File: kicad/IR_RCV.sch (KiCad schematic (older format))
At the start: 9 parts, among them J1 Host, J2 Slave, Q1 MTM231232LBF, Q2 DMN3065LW-7, Q3 SFH3015FA

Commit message: 部品を配置 kicad5
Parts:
- removed J1: Host, mouse:STAND_HOST_05, symbol Conn_01x05_Female
- removed J2: Slave, mouse:STAND_SLAVE_05, symbol Conn_01x05_Male
- added J15: Host, mouse:STAND_HOST_05, symbol Connector:Conn_01x05_Female
- added J16: Slave, mouse:STAND_SLAVE_05, symbol Connector:Conn_01x05_Male
- C6: symbol C -> Device:C
- D3: symbol LED -> Device:LED
- Q1: symbol Q_PMOS_GSD -> Device:Q_PMOS_GSD
- Q2: symbol Q_NMOS_GSD -> Device:Q_NMOS_GSD
- Q3: symbol Q_Photo_NPN -> Device:Q_Photo_NPN
- R6, R7: symbol R -> Device:R
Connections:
- net +3V3: now also J15.1 (Pin_1)
- net GND: now also J15.5 (Pin_5)
- net IR_LED: now also J15.3 (Pin_3)
- net IR_RCV: now also J15.4 (Pin_4)
- net VDDA: now also J15.2 (Pin_2)
- net s_3.3V: now also J16.1 (Pin_1)
- net s_AVDD: now also J16.2 (Pin_2)
- net s_GND: now also J16.5 (Pin_5)
- net s_IR_LED: now also J16.3 (Pin_3)
- net s_IR_RCV: now also J16.4 (Pin_4)
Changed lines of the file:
@@
-EESchema Schematic File Version 2
-LIBS:power
-LIBS:device
-LIBS:transistors
-LIBS:conn
-LIBS:linear
-LIBS:regul
-LIBS:74xx
-LIBS:cmos4000
-LIBS:adc-dac
-LIBS:memory
-LIBS:xilinx
-LIBS:microcontrollers
-LIBS:dsp
-LIBS:microchip
-LIBS:analog_switches
-LIBS:motorola
-LIBS:texas
-LIBS:intel
-LIBS:audio
-LIBS:interface
-LIBS:digital-audio
-LIBS:philips
-LIBS:display
-LIBS:cypress
-LIBS:siliconi
-LIBS:opto
-LIBS:atmel
-LIBS:contrib
-LIBS:valves
-LIBS:KERISE
-LIBS:74xgxx
-LIBS:ac-dc
-LIBS:actel
-LIBS:allegro
-LIBS:Altera
-LIBS:analog_devices
-LIBS:battery_management
-LIBS:bbd
-LIBS:bosch
-LIBS:brooktre
-LIBS:cmos_ieee
-LIBS:dc-dc
-LIBS:diode
-LIBS:elec-unifil
-LIBS:ESD_Protection
-LIBS:ftdi
-LIBS:gennum
-LIBS:hc11
-LIBS:ir
-LIBS:Lattice
-LIBS:leds
-LIBS:maxim
-LIBS:mechanical
-LIBS:microchip_dspic33dsc
-LIBS:microchip_pic10mcu
-LIBS:microchip_pic12mcu
-LIBS:microchip_pic16mcu
-LIBS:microchip_pic18mcu
-LIBS:microchip_pic24mcu
-LIBS:microchip_pic32mcu
-LIBS:modules
-LIBS:motor_drivers
-LIBS:motors
-LIBS:msp430
-LIBS:nordicsemi
-LIBS:nxp
-LIBS:nxp_armmcu
-LIBS:onsemi
-LIBS:Oscillators
-LIBS:Power_Management
-LIBS:powerint
-LIBS:pspice
-LIBS:references
-LIBS:relays
-LIBS:rfcom
-LIBS:sensors
-LIBS:silabs
-LIBS:stm8
-LIBS:stm32
-LIBS:supertex
-LIBS:switches
-LIBS:transf
-LIBS:triac_thyristor
-LIBS:ttl_ieee
-LIBS:video
-LIBS:wiznet
-LIBS:Worldsemi
-LIBS:Xicor
-LIBS:zetex
-LIBS:Zilog
-LIBS:graphic_symbols
-LIBS:infineon
-LIBS:intersil
-LIBS:LEM
-LIBS:logic_programmable
-LIBS:RFSolutions
+EESchema Schematic File Version 4
 LIBS:KERISE-cache
-EELAYER 25 0
+EELAYER 26 0
 EELAYER END
 $Descr A4 11693 8268
 encoding utf-8
-Sheet 13 15
+Sheet 12 14
 Title ""
 Date ""
@@
 Photo Reflector v20180503\nKERI's Lab
 $Comp
-L Q_NMOS_GSD Q2
+L Device:Q_NMOS_GSD Q2
 U 1 1 589BE75A
 P 4300 5500
@@
 AR Path="/597E1B35/589BE75A" Ref="Q9"  Part="1"
 AR Path="/597E1B39/589BE75A" Ref="Q12"  Part="1"
-F 0 "Q5" H 4300 5650 50  0000 R CNN
+F 0 "Q12" H 4300 5650 50  0000 R CNN
 F 1 "DMN3065LW-7" H 4350 5350 50  0000 R CNN
 F 2 "TO_SOT_Packages_SMD:SOT-323_SC-70" H 4500 5600 50  0001 C CNN
@@
 $EndComp
 $Comp
-L R R6
+L Device:R R6
 U 1 1 589BE76D
 P 4400 4450
 AR Path="/57CF0B09/589BE76D" Ref="R6"  Part="1"
 AR Path="/57CF2A30/589BE76D" Ref="R8"  Part="1"
-AR Path="/597E1B35/589BE76D" Ref="R13"  Part="1"
-AR Path="/597E1B39/589BE76D" Ref="R15"  Part="1"
-F 0 "R8" V 4480 4450 50  0000 C CNN
+AR Path="/597E1B35/589BE76D" Ref="R11"  Part="1"
+AR Path="/597E1B39/589BE76D" Ref="R13"  Part="1"
+F 0 "R13" V 4480 4450 50  0000 C CNN
 F 1 "100" V 4400 4450 50  0000 C CNN
 F 2 "Resistors_SMD:R_0603" V 4330 4450 50  0001 C CNN
@@
 IR_LED
 $Comp
-L GND #PWR036
+L power:GND #PWR035
 U 1 1 589BF265
 P 4400 2600
-AR Path="/57CF0B09/589BF265" Ref="#PWR036"  Part="1"
-AR Path="/57CF2A30/589BF265" Ref="#PWR039"  Part="1"
-AR Path="/597E1B35/589BF265" Ref="#PWR063"  Part="1"
-AR Path="/597E1B39/589BF265" Ref="#PWR066"  Part="1"
-F 0 "#PWR066" H 4400 2350 50  0001 C CNN
+AR Path="/57CF0B09/589BF265" Ref="#PWR035"  Part="1"
+AR Path="/57CF2A30/589BF265" Ref="#PWR038"  Part="1"
+AR Path="/597E1B35/589BF265" Ref="#PWR054"  Part="1"
+AR Path="/597E1B39/589BF265" Ref="#PWR057"  Part="1"
+F 0 "#PWR057" H 4400 2350 50  0001 C CNN
 F 1 "GND" H 4400 2450 50  0000 C CNN
 F 2 "" H 4400 2600 50  0000 C CNN
@@
 	4100 2000 4100 2200
 Wire Wire Line
-	4400 4800 4400 4600
+	4400 4800 4400 4700
 Wire Wire Line
 	5600 5700 5600 6000
@@
 s_AVDD
 $Comp
-L LED D3
+L Device:LED D3
 U 1 1 594AC674
 P 4400 4950
@@
 AR Path="/597E1B35/594AC674" Ref="D5"  Part="1"
 AR Path="/597E1B39/594AC674" Ref="D6"  Part="1"
-F 0 "D4" V 4500 4800 50  0000 C CNN
+F 0 "D6" V 4500 4800 50  0000 C CNN
 F 1 "SFH4045N" V 4400 4650 50  0000 C CNN
 F 2 "mouse:SFH4045N" H 4400 4950 50  0001 C CNN
@@
 $EndComp
 $Comp
-L VDDA #PWR037
+L power:VDDA #PWR033
 U 1 1 59C54857
 P 4100 2000
-AR Path="/57CF0B09/59C54857" Ref="#PWR037"  Part="1"
-AR Path="/57CF2A30/59C54857" Ref="#PWR040"  Part="1"
-AR Path="/597E1B35/59C54857" Ref="#PWR064"  Part="1"
-AR Path="/597E1B39/59C54857" Ref="#PWR067"  Part="1"
-F 0 "#PWR067" H 4100 1850 50  0001 C CNN
+AR Path="/57CF0B09/59C54857" Ref="#PWR033"  Part="1"
+AR Path="/57CF2A30/59C54857" Ref="#PWR036"  Part="1"
+AR Path="/597E1B35/59C54857" Ref="#PWR052"  Part="1"
+AR Path="/597E1B39/59C54857" Ref="#PWR055"  Part="1"
+F 0 "#PWR055" H 4100 1850 50  0001 C CNN
 F 1 "VDDA" H 4100 2150 50  0000 C CNN
 F 2 "" H 4100 2000 50  0001 C CNN
@@
 $EndComp
 $Comp
-L Conn_01x05_Female J1
-U 1 1 5A172E6D
-P 4700 2300
-AR Path="/57CF0B09/5A172E6D" Ref="J1"  Part="1"
-AR Path="/57CF2A30/5A172E6D" Ref="J3"  Part="1"
-AR Path="/597E1B35/5A172E6D" Ref="J6"  Part="1"
-AR Path="/597E1B39/5A172E6D" Ref="J8"  Part="1"
-F 0 "J3" H 4700 2600 50  0000 C CNN
-F 1 "Host" H 4700 2000 50  0000 C CNN
-F 2 "mouse:STAND_HOST_05" H 4700 2300 50  0001 C CNN
-F 3 "" H 4700 2300 50  0001 C CNN
-	1    4700 2300
-	1    0    0    -1
-$EndComp
-$Comp
-L +3.3V #PWR038
+L power:+3.3V #PWR034
 U 1 1 5A172FEF
 P 4400 2000
-AR Path="/57CF0B09/5A172FEF" Ref="#PWR038"  Part="1"
-AR Path="/57CF2A30/5A172FEF" Ref="#PWR041"  Part="1"
-AR Path="/597E1B35/5A172FEF" Ref="#PWR065"  Part="1"
-AR Path="/597E1B39/5A172FEF" Ref="#PWR068"  Part="1"
-F 0 "#PWR068" H 4400 1850 50  0001 C CNN
+AR Path="/57CF0B09/5A172FEF" Ref="#PWR034"  Part="1"
+AR Path="/57CF2A30/5A172FEF" Ref="#PWR037"  Part="1"
+AR Path="/597E1B35/5A172FEF" Ref="#PWR053"  Part="1"
+AR Path="/597E1B39/5A172FEF" Ref="#PWR056"  Part="1"
+F 0 "#PWR056" H 4400 1850 50  0001 C CNN
 F 1 "+3.3V" H 4400 2140 50  0000 C CNN
 F 2 "" H 4400 2000 50  0001 C CNN
@@
 Wire Wire Line
 	4500 2400 4400 2400
-$Comp
-L Conn_01x05_Male J2
-U 1 1 5A17311F
-P 5000 2300
-AR Path="/57CF0B09/5A17311F" Ref="J2"  Part="1"
-AR Path="/57CF2A30/5A17311F" Ref="J4"  Part="1"
-AR Path="/597E1B35/5A17311F" Ref="J7"  Part="1"
-AR Path="/597E1B39/5A17311F" Ref="J9"  Part="1"
-F 0 "J4" H 5000 2600 50  0000 C CNN
-F 1 "Slave" H 5000 2000 50  0000 C CNN
-F 2 "mouse:STAND_SLAVE_05" H 5000 2300 50  0001 C CNN
-F 3 "" H 5000 2300 50  0001 C CNN
-	1    5000 2300
-	1    0    0    -1
-$EndComp
 Wire Wire Line
 	5300 2500 5200 2500
@@
 s_AVDD
 $Comp
-L C C6
+L Device:C C6
 U 1 1 5A1B992B
 P 5000 5550
 AR Path="/57CF0B09/5A1B992B" Ref="C6"  Part="1"
 AR Path="/57CF2A30/5A1B992B" Ref="C7"  Part="1"
-AR Path="/597E1B35/5A1B992B" Ref="C14"  Part="1"
-AR Path="/597E1B39/5A1B992B" Ref="C15"  Part="1"
-F 0 "C7" H 5025 5650 50  0000 L CNN
+AR Path="/597E1B35/5A1B992B" Ref="C12"  Part="1"
+AR Path="/597E1B39/5A1B992B" Ref="C13"  Part="1"
+F 0 "C13" H 5025 5650 50  0000 L CNN
 F 1 "1u" H 5025 5450 50  0000 L CNN
 F 2 "Capacitors_SMD:C_0402_NoSilk" H 5038 5400 50  0001 C CNN
@@
 $EndComp
 $Comp
-L Q_Photo_NPN Q3
+L Device:Q_Photo_NPN Q3
 U 1 1 5A4ADF8B
 P 5500 4400
@@
 AR Path="/597E1B35/5A4ADF8B" Ref="Q10"  Part="1"
 AR Path="/597E1B39/5A4ADF8B" Ref="Q13"  Part="1"
-F 0 "Q6" H 5700 4450 50  0000 L CNN
+F 0 "Q13" H 5700 4450 50  0000 L CNN
 F 1 "SFH3015FA" H 5700 4350 50  0000 L CNN
 F 2 "mouse:SFH3015FA" H 5700 4500 50  0001 C CNN
@@
 $EndComp
 $Comp
-L R R7
+L Device:R R7
 U 1 1 589BEE3B
 P 5600 5550
 AR Path="/57CF0B09/589BEE3B" Ref="R7"  Part="1"
 AR Path="/57CF2A30/589BEE3B" Ref="R9"  Part="1"
-AR Path="/597E1B35/589BEE3B" Ref="R14"  Part="1"
-AR Path="/597E1B39/589BEE3B" Ref="R16"  Part="1"
-F 0 "R9" V 5680 5550 50  0000 C CNN
+AR Path="/597E1B35/589BEE3B" Ref="R12"  Part="1"
+AR Path="/597E1B39/589BEE3B" Ref="R14"  Part="1"
+F 0 "R14" V 5680 5550 50  0000 C CNN
 F 1 "10k" V 5600 5550 50  0000 C CNN
 F 2 "Resistors_SMD:R_0201_NoSilk" V 5530 5550 50  0001 C CNN
@@
 	3400 6100 6200 6100
 $Comp
-L Q_PMOS_GSD Q1
+L Device:Q_PMOS_GSD Q1
 U 1 1 5AB4DD07
 P 4300 4000
@@
 AR Path="/597E1B35/5AB4DD07" Ref="Q8"  Part="1"
 AR Path="/597E1B39/5AB4DD07" Ref="Q11"  Part="1"
-F 0 "Q4" H 4500 4050 50  0000 L CNN
+F 0 "Q11" H 4500 4050 50  0000 L CNN
 F 1 "MTM231232LBF" H 4500 3950 50  0000 L CNN
 F 2 "TO_SOT_Packages_SMD:SOT-323_SC-70" H 4500 4100 50  0001 C CNN
@@
 	4400 3700 4400 3800
 Wire Wire Line
-	3900 5500 4100 5500
+	3900 5500 4000 5500
 Wire Wire Line
 	4100 4000 4000 4000
@@
 	4000 4000 4000 5500
 Wire Wire Line
-	5600 5400 5600 4600
+	5600 5400 5600 4800
 Connection ~ 4000 5500
 Wire Notes Line
@@
 Wire Notes Line
 	6200 3300 6200 6100
+Wire Wire Line
+	4400 4700 4400 4600
+Wire Wire Line
+	5600 4800 5600 4600
+Wire Wire Line
+	4000 5500 4100 5500
+$Comp
+L Connector:Conn_01x05_Female J15
+U 1 1 5B6F3B71
+P 4700 2300
+AR Path="/597E1B39/5B6F3B71" Ref="J15"  Part="1"
+AR Path="/597E1B35/5B6F3B71" Ref="J13"  Part="1"
+AR Path="/57CF0B09/5B6F3B71" Ref="J3"  Part="1"
+AR Path="/57CF2A30/5B6F3B71" Ref="J5"  Part="1"
+F 0 "J15" H 4728 2326 50  0000 L CNN
+F 1 "Host" H 4728 2235 50  0000 L CNN
+F 2 "mouse:STAND_HOST_05" H 4700 2300 50  0001 C CNN
+F 3 "~" H 4700 2300 50  0001 C CNN
+	1    4700 2300
+	1    0    0    -1
+$EndComp
+$Comp
+L Connector:Conn_01x05_Male J16
+U 1 1 5B6F3C20
+P 5000 2300
+AR Path="/597E1B39/5B6F3C20" Ref="J16"  Part="1"
+AR Path="/597E1B35/5B6F3C20" Ref="J14"  Part="1"
+AR Path="/57CF0B09/5B6F3C20" Ref="J4"  Part="1"
+AR Path="/57CF2A30/5B6F3C20" Ref="J6"  Part="1"
+F 0 "J16" H 5106 2678 50  0000 C CNN
+F 1 "Slave" H 5106 2587 50  0000 C CNN
+F 2 "mouse:STAND_SLAVE_05" H 5000 2300 50  0001 C CNN
+F 3 "~" H 5000 2300 50  0001 C CNN
+	1    5000 2300
+	1    0    0    -1
+$EndComp
 $EndSCHEMATC

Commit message: コンデンサを追加
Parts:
- renumbered C6 to C7
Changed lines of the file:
@@
 IR_LED
 $Comp
-L power:GND #PWR035
+L power:GND #PWR037
 U 1 1 589BF265
 P 4400 2600
-AR Path="/57CF0B09/589BF265" Ref="#PWR035"  Part="1"
-AR Path="/57CF2A30/589BF265" Ref="#PWR038"  Part="1"
-AR Path="/597E1B35/589BF265" Ref="#PWR054"  Part="1"
-AR Path="/597E1B39/589BF265" Ref="#PWR057"  Part="1"
-F 0 "#PWR057" H 4400 2350 50  0001 C CNN
+AR Path="/57CF0B09/589BF265" Ref="#PWR037"  Part="1"
+AR Path="/57CF2A30/589BF265" Ref="#PWR040"  Part="1"
+AR Path="/597E1B35/589BF265" Ref="#PWR056"  Part="1"
+AR Path="/597E1B39/589BF265" Ref="#PWR059"  Part="1"
+F 0 "#PWR059" H 4400 2350 50  0001 C CNN
 F 1 "GND" H 4400 2450 50  0000 C CNN
 F 2 "" H 4400 2600 50  0000 C CNN
@@
 $EndComp
 $Comp
-L power:VDDA #PWR033
+L power:VDDA #PWR035
 U 1 1 59C54857
 P 4100 2000
-AR Path="/57CF0B09/59C54857" Ref="#PWR033"  Part="1"
-AR Path="/57CF2A30/59C54857" Ref="#PWR036"  Part="1"
-AR Path="/597E1B35/59C54857" Ref="#PWR052"  Part="1"
-AR Path="/597E1B39/59C54857" Ref="#PWR055"  Part="1"
-F 0 "#PWR055" H 4100 1850 50  0001 C CNN
+AR Path="/57CF0B09/59C54857" Ref="#PWR035"  Part="1"
+AR Path="/57CF2A30/59C54857" Ref="#PWR038"  Part="1"
+AR Path="/597E1B35/59C54857" Ref="#PWR054"  Part="1"
+AR Path="/597E1B39/59C54857" Ref="#PWR057"  Part="1"
+F 0 "#PWR057" H 4100 1850 50  0001 C CNN
 F 1 "VDDA" H 4100 2150 50  0000 C CNN
 F 2 "" H 4100 2000 50  0001 C CNN
@@
 $EndComp
 $Comp
-L power:+3.3V #PWR034
+L power:+3.3V #PWR036
 U 1 1 5A172FEF
 P 4400 2000
-AR Path="/57CF0B09/5A172FEF" Ref="#PWR034"  Part="1"
-AR Path="/57CF2A30/5A172FEF" Ref="#PWR037"  Part="1"
-AR Path="/597E1B35/5A172FEF" Ref="#PWR053"  Part="1"
-AR Path="/597E1B39/5A172FEF" Ref="#PWR056"  Part="1"
-F 0 "#PWR056" H 4400 1850 50  0001 C CNN
+AR Path="/57CF0B09/5A172FEF" Ref="#PWR036"  Part="1"
+AR Path="/57CF2A30/5A172FEF" Ref="#PWR039"  Part="1"
+AR Path="/597E1B35/5A172FEF" Ref="#PWR055"  Part="1"
+AR Path="/597E1B39/5A172FEF" Ref="#PWR058"  Part="1"
+F 0 "#PWR058" H 4400 1850 50  0001 C CNN
 F 1 "+3.3V" H 4400 2140 50  0000 C CNN
 F 2 "" H 4400 2000 50  0001 C CNN
@@
 s_AVDD
 $Comp
-L Device:C C6
+L Device:C C7
 U 1 1 5A1B992B
 P 5000 5550
-AR Path="/57CF0B09/5A1B992B" Ref="C6"  Part="1"
-AR Path="/57CF2A30/5A1B992B" Ref="C7"  Part="1"
-AR Path="/597E1B35/5A1B992B" Ref="C12"  Part="1"
-AR Path="/597E1B39/5A1B992B" Ref="C13"  Part="1"
-F 0 "C13" H 5025 5650 50  0000 L CNN
+AR Path="/57CF0B09/5A1B992B" Ref="C7"  Part="1"
+AR Path="/57CF2A30/5A1B992B" Ref="C8"  Part="1"
+AR Path="/597E1B35/5A1B992B" Ref="C13"  Part="1"
+AR Path="/597E1B39/5A1B992B" Ref="C14"  Part="1"
+F 0 "C14" H 5025 5650 50  0000 L CNN
 F 1 "1u" H 5025 5450 50  0000 L CNN
 F 2 "Capacitors_SMD:C_0402_NoSilk" H 5038 5400 50  0001 C CNN

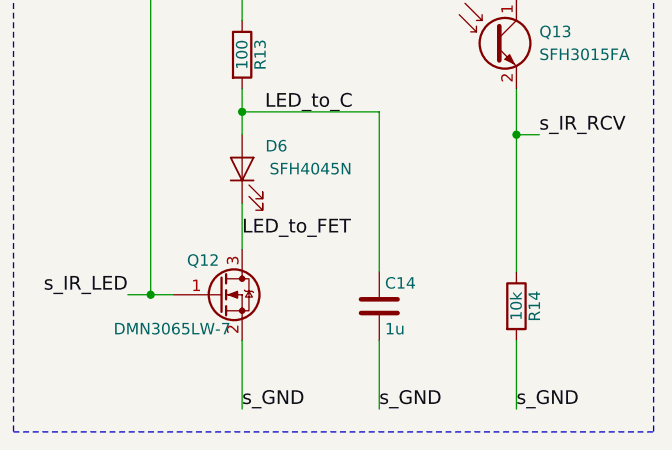
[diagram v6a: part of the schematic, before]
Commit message: KERISEv4-5に向けて回路図を更新
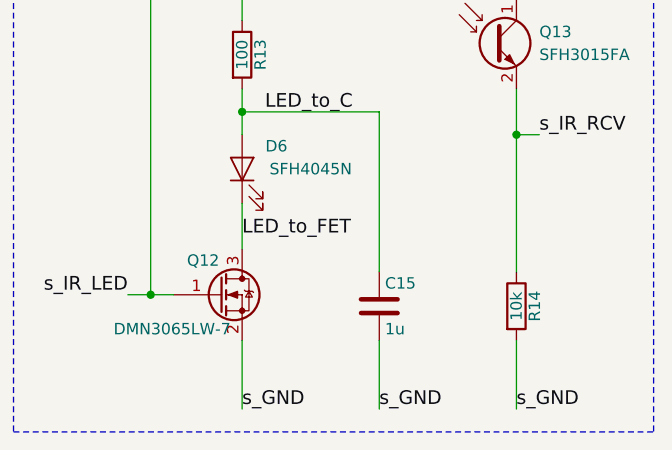
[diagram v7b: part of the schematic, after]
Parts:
- renumbered C7 to C8
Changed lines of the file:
@@
 $Descr A4 11693 8268
 encoding utf-8
-Sheet 12 14
+Sheet 12 15
 Title ""
 Date ""
@@
 IR_LED
 $Comp
-L power:GND #PWR037
+L power:GND #PWR039
 U 1 1 589BF265
 P 4400 2600
-AR Path="/57CF0B09/589BF265" Ref="#PWR037"  Part="1"
-AR Path="/57CF2A30/589BF265" Ref="#PWR040"  Part="1"
-AR Path="/597E1B35/589BF265" Ref="#PWR056"  Part="1"
-AR Path="/597E1B39/589BF265" Ref="#PWR059"  Part="1"
-F 0 "#PWR059" H 4400 2350 50  0001 C CNN
+AR Path="/57CF0B09/589BF265" Ref="#PWR039"  Part="1"
+AR Path="/57CF2A30/589BF265" Ref="#PWR042"  Part="1"
+AR Path="/597E1B35/589BF265" Ref="#PWR058"  Part="1"
+AR Path="/597E1B39/589BF265" Ref="#PWR061"  Part="1"
+F 0 "#PWR061" H 4400 2350 50  0001 C CNN
 F 1 "GND" H 4400 2450 50  0000 C CNN
 F 2 "" H 4400 2600 50  0000 C CNN
@@
 $EndComp
 $Comp
-L power:VDDA #PWR035
+L power:VDDA #PWR037
 U 1 1 59C54857
 P 4100 2000
-AR Path="/57CF0B09/59C54857" Ref="#PWR035"  Part="1"
-AR Path="/57CF2A30/59C54857" Ref="#PWR038"  Part="1"
-AR Path="/597E1B35/59C54857" Ref="#PWR054"  Part="1"
-AR Path="/597E1B39/59C54857" Ref="#PWR057"  Part="1"
-F 0 "#PWR057" H 4100 1850 50  0001 C CNN
+AR Path="/57CF0B09/59C54857" Ref="#PWR037"  Part="1"
+AR Path="/57CF2A30/59C54857" Ref="#PWR040"  Part="1"
+AR Path="/597E1B35/59C54857" Ref="#PWR056"  Part="1"
+AR Path="/597E1B39/59C54857" Ref="#PWR059"  Part="1"
+F 0 "#PWR059" H 4100 1850 50  0001 C CNN
 F 1 "VDDA" H 4100 2150 50  0000 C CNN
 F 2 "" H 4100 2000 50  0001 C CNN
@@
 $EndComp
 $Comp
-L power:+3.3V #PWR036
+L power:+3.3V #PWR038
 U 1 1 5A172FEF
 P 4400 2000
-AR Path="/57CF0B09/5A172FEF" Ref="#PWR036"  Part="1"
-AR Path="/57CF2A30/5A172FEF" Ref="#PWR039"  Part="1"
-AR Path="/597E1B35/5A172FEF" Ref="#PWR055"  Part="1"
-AR Path="/597E1B39/5A172FEF" Ref="#PWR058"  Part="1"
-F 0 "#PWR058" H 4400 1850 50  0001 C CNN
+AR Path="/57CF0B09/5A172FEF" Ref="#PWR038"  Part="1"
+AR Path="/57CF2A30/5A172FEF" Ref="#PWR041"  Part="1"
+AR Path="/597E1B35/5A172FEF" Ref="#PWR057"  Part="1"
+AR Path="/597E1B39/5A172FEF" Ref="#PWR060"  Part="1"
+F 0 "#PWR060" H 4400 1850 50  0001 C CNN
 F 1 "+3.3V" H 4400 2140 50  0000 C CNN
 F 2 "" H 4400 2000 50  0001 C CNN
@@
 s_AVDD
 $Comp
-L Device:C C7
+L Device:C C8
 U 1 1 5A1B992B
 P 5000 5550
-AR Path="/57CF0B09/5A1B992B" Ref="C7"  Part="1"
-AR Path="/57CF2A30/5A1B992B" Ref="C8"  Part="1"
-AR Path="/597E1B35/5A1B992B" Ref="C13"  Part="1"
-AR Path="/597E1B39/5A1B992B" Ref="C14"  Part="1"
-F 0 "C14" H 5025 5650 50  0000 L CNN
+AR Path="/57CF0B09/5A1B992B" Ref="C8"  Part="1"
+AR Path="/57CF2A30/5A1B992B" Ref="C9"  Part="1"
+AR Path="/597E1B35/5A1B992B" Ref="C14"  Part="1"
+AR Path="/597E1B39/5A1B992B" Ref="C15"  Part="1"
+F 0 "C15" H 5025 5650 50  0000 L CNN
 F 1 "1u" H 5025 5450 50  0000 L CNN
 F 2 "Capacitors_SMD:C_0402_NoSilk" H 5038 5400 50  0001 C CNN

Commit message: フットプリントを割り当て
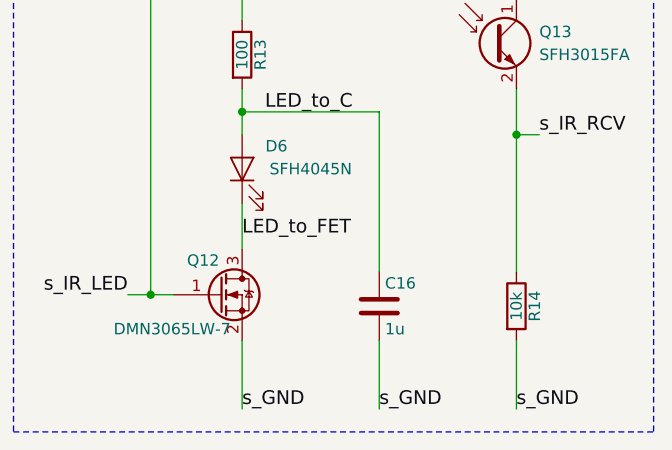
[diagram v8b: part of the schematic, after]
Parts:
- C9: renamed from C8; footprint Capacitors_SMD:C_0402_NoSilk -> Capacitor_SMD:C_0402_1005Metric
- R6: footprint Resistors_SMD:R_0603 -> Resistor_SMD:R_0603_1608Metric
- R7: footprint Resistors_SMD:R_0201_NoSilk -> Resistor_SMD:R_0201_0603Metric
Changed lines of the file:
@@
 F 0 "R13" V 4480 4450 50  0000 C CNN
 F 1 "100" V 4400 4450 50  0000 C CNN
-F 2 "Resistors_SMD:R_0603" V 4330 4450 50  0001 C CNN
+F 2 "Resistor_SMD:R_0603_1608Metric" V 4330 4450 50  0001 C CNN
 F 3 "" H 4400 4450 50  0000 C CNN
 	1    4400 4450
@@
 IR_LED
 $Comp
-L power:GND #PWR039
+L power:GND #PWR041
 U 1 1 589BF265
 P 4400 2600
-AR Path="/57CF0B09/589BF265" Ref="#PWR039"  Part="1"
-AR Path="/57CF2A30/589BF265" Ref="#PWR042"  Part="1"
-AR Path="/597E1B35/589BF265" Ref="#PWR058"  Part="1"
-AR Path="/597E1B39/589BF265" Ref="#PWR061"  Part="1"
-F 0 "#PWR061" H 4400 2350 50  0001 C CNN
+AR Path="/57CF0B09/589BF265" Ref="#PWR041"  Part="1"
+AR Path="/57CF2A30/589BF265" Ref="#PWR044"  Part="1"
+AR Path="/597E1B35/589BF265" Ref="#PWR060"  Part="1"
+AR Path="/597E1B39/589BF265" Ref="#PWR063"  Part="1"
+F 0 "#PWR063" H 4400 2350 50  0001 C CNN
 F 1 "GND" H 4400 2450 50  0000 C CNN
 F 2 "" H 4400 2600 50  0000 C CNN
@@
 $EndComp
 $Comp
-L power:VDDA #PWR037
+L power:VDDA #PWR039
 U 1 1 59C54857
 P 4100 2000
-AR Path="/57CF0B09/59C54857" Ref="#PWR037"  Part="1"
-AR Path="/57CF2A30/59C54857" Ref="#PWR040"  Part="1"
-AR Path="/597E1B35/59C54857" Ref="#PWR056"  Part="1"
-AR Path="/597E1B39/59C54857" Ref="#PWR059"  Part="1"
-F 0 "#PWR059" H 4100 1850 50  0001 C CNN
+AR Path="/57CF0B09/59C54857" Ref="#PWR039"  Part="1"
+AR Path="/57CF2A30/59C54857" Ref="#PWR042"  Part="1"
+AR Path="/597E1B35/59C54857" Ref="#PWR058"  Part="1"
+AR Path="/597E1B39/59C54857" Ref="#PWR061"  Part="1"
+F 0 "#PWR061" H 4100 1850 50  0001 C CNN
 F 1 "VDDA" H 4100 2150 50  0000 C CNN
 F 2 "" H 4100 2000 50  0001 C CNN
@@
 $EndComp
 $Comp
-L power:+3.3V #PWR038
+L power:+3.3V #PWR040
 U 1 1 5A172FEF
 P 4400 2000
-AR Path="/57CF0B09/5A172FEF" Ref="#PWR038"  Part="1"
-AR Path="/57CF2A30/5A172FEF" Ref="#PWR041"  Part="1"
-AR Path="/597E1B35/5A172FEF" Ref="#PWR057"  Part="1"
-AR Path="/597E1B39/5A172FEF" Ref="#PWR060"  Part="1"
-F 0 "#PWR060" H 4400 1850 50  0001 C CNN
+AR Path="/57CF0B09/5A172FEF" Ref="#PWR040"  Part="1"
+AR Path="/57CF2A30/5A172FEF" Ref="#PWR043"  Part="1"
+AR Path="/597E1B35/5A172FEF" Ref="#PWR059"  Part="1"
+AR Path="/597E1B39/5A172FEF" Ref="#PWR062"  Part="1"
+F 0 "#PWR062" H 4400 1850 50  0001 C CNN
 F 1 "+3.3V" H 4400 2140 50  0000 C CNN
 F 2 "" H 4400 2000 50  0001 C CNN
@@
 s_AVDD
 $Comp
-L Device:C C8
+L Device:C C9
 U 1 1 5A1B992B
 P 5000 5550
-AR Path="/57CF0B09/5A1B992B" Ref="C8"  Part="1"
-AR Path="/57CF2A30/5A1B992B" Ref="C9"  Part="1"
-AR Path="/597E1B35/5A1B992B" Ref="C14"  Part="1"
-AR Path="/597E1B39/5A1B992B" Ref="C15"  Part="1"
-F 0 "C15" H 5025 5650 50  0000 L CNN
+AR Path="/57CF0B09/5A1B992B" Ref="C9"  Part="1"
+AR Path="/57CF2A30/5A1B992B" Ref="C10"  Part="1"
+AR Path="/597E1B35/5A1B992B" Ref="C15"  Part="1"
+AR Path="/597E1B39/5A1B992B" Ref="C16"  Part="1"
+F 0 "C16" H 5025 5650 50  0000 L CNN
 F 1 "1u" H 5025 5450 50  0000 L CNN
-F 2 "Capacitors_SMD:C_0402_NoSilk" H 5038 5400 50  0001 C CNN
+F 2 "Capacitor_SMD:C_0402_1005Metric" H 5038 5400 50  0001 C CNN
 F 3 "" H 5000 5550 50  0001 C CNN
 	1    5000 5550
@@
 F 0 "R14" V 5680 5550 50  0000 C CNN
 F 1 "10k" V 5600 5550 50  0000 C CNN
-F 2 "Resistors_SMD:R_0201_NoSilk" V 5530 5550 50  0001 C CNN
+F 2 "Resistor_SMD:R_0201_0603Metric" V 5530 5550 50  0001 C CNN
 F 3 "" H 5600 5550 50  0000 C CNN
 	1    5600 5550
